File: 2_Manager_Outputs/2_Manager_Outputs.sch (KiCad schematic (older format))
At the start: 83 parts, among them J1 Jumper, J10 Jumper, J11 Jumper, J12 Jumper, J13 Jumper, J14 Jumper, J15 Jumper, J16 Jumper, J2 Jumper, J3 Jumper, J4 Jumper, J5 Jumper, J6 Jumper, J7 Jumper, J8 Jumper, J9 Jumper, P1 MCLK_EXTERNAL, P2 CONN_01X04, P3 SPI_AD5270_1, P4 CONN_01X04, P5 SPI_AD5270_2, P6 SPI_AD9833_1, P7 SPI_AD9833_2, U1 ATMEGA328P-AU, U10 ADP3334, U11 LD1117S50TR, U2 AD8421, U3 AD9833, U6 AD8421, U8 AD9833, U9 ADG819

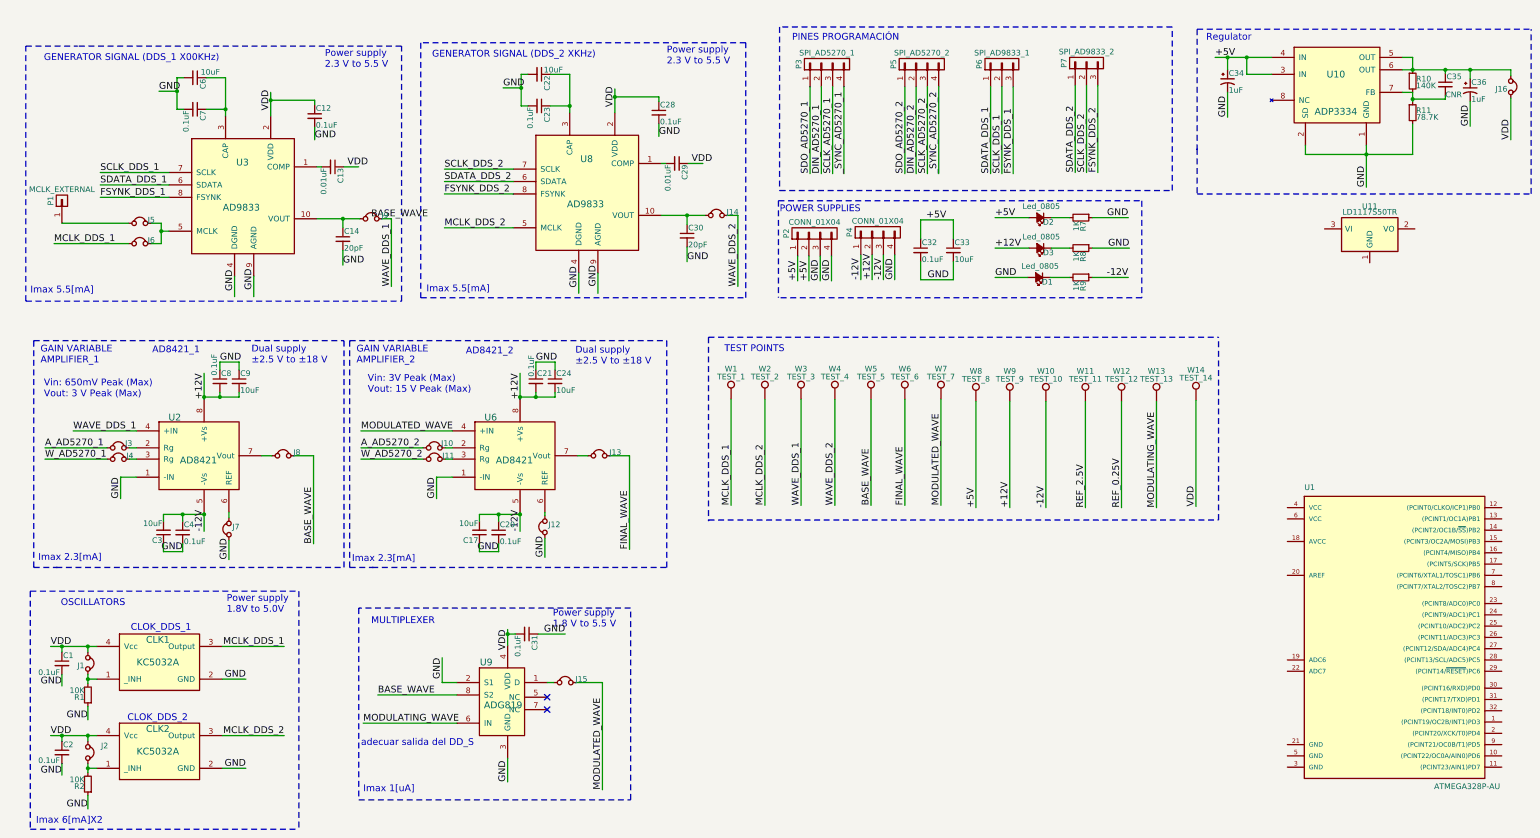
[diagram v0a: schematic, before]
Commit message: //
Plantilla para hacer tanto la pcb de manager output como la pcb de wave
generator// Separar el diseño en dos y empezar a trabajar por aparte
cada pcb
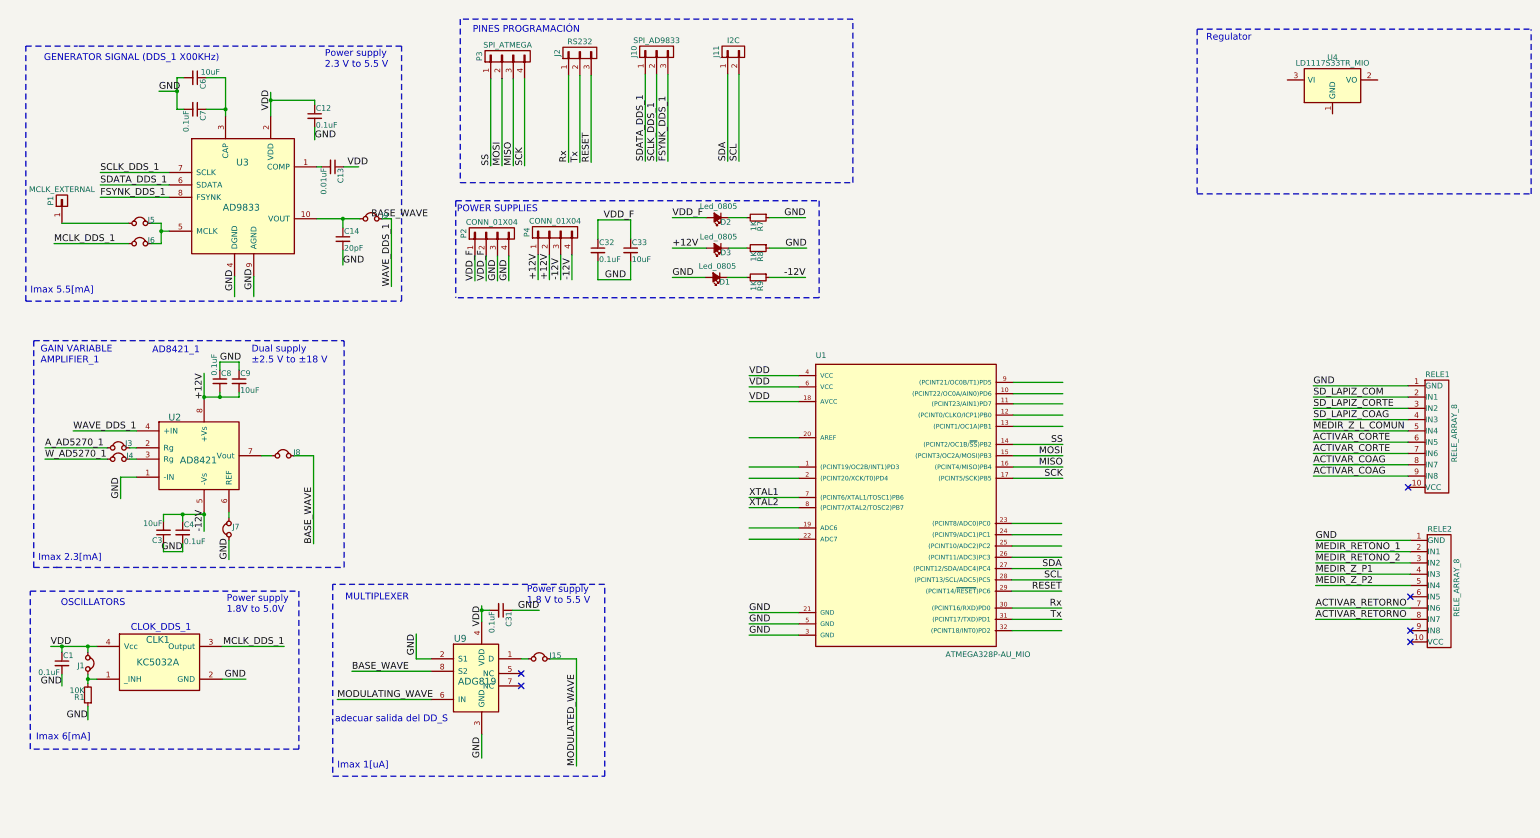
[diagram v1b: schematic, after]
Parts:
- removed C17, C24: 10uF, Capacitors_SMD:C_1206_HandSoldering, symbol 10uF
- removed C2, C20, C21, C23, C28: 0.1uF, Capacitors_SMD:C_0805_HandSoldering, symbol 0.1uF
- removed C22: 10uF, Capacitors_SMD:C_0805_HandSoldering, symbol 10uF
- removed C29: 0.01uF, Capacitors_SMD:C_0805_HandSoldering, symbol 0.01uF
- removed C30: 20pF, Capacitors_SMD:C_0805_HandSoldering, symbol 20pF
- removed C34, C36: 1uF, Capacitors_SMD:C_0805_HandSoldering, symbol CP1_Small
- removed C35: CNR, Capacitors_SMD:C_1206_HandSoldering, symbol C_Small
- removed CLK2: KC5032A, Foot_Prints_PCB_OSCILLATOR:KC5032A_Foot_Print, symbol KC5032A
- removed J10, J11, J12, J13, J14, J16, J2: Jumper, Pin_Headers:Pin_Header_Straight_1x02, symbol Jumper-RESCUE-PCB_OSCILLATOR
- removed P5: SPI_AD5270_2, Socket_Strips:Socket_Strip_Straight_1x04, symbol CONN_01X04
- removed P6: SPI_AD9833_1, Socket_Strips:Socket_Strip_Straight_1x03, symbol CONN_01X03
- removed P7: SPI_AD9833_2, Socket_Strips:Socket_Strip_Straight_1x03, symbol CONN_01X03
- removed R10: 140K, Resistors_SMD:R_0805_HandSoldering, symbol R_Small
- removed R11: 78.7K, Resistors_SMD:R_0805_HandSoldering, symbol R_Small
- removed R2: 10K, Resistors_SMD:R_0805_HandSoldering, symbol 10K
- removed U1: ATMEGA328P-AU, Housings_QFP:TQFP-32_7x7mm_Pitch0.8mm, symbol ATMEGA328P-AU
- removed U10: ADP3334, Housings_SOIC:SOIC-8_3.9x4.9mm_Pitch1.27mm, symbol ADP3334
- removed U11: LD1117S50TR, TO_SOT_Packages_SMD:SOT-223, symbol LD1117S50TR
- removed U6: AD8421, Housings_SOIC:SOIC-8_3.9x4.9mm_Pitch1.27mm, symbol AD8421
- removed U8: AD9833, Housings_SSOP:MSOP-10_3x3mm_Pitch0.5mm, symbol AD9833
- removed W1: TEST_1, Measurement_Points:Measurement_Point_Round-TH_Small, symbol TEST_1P
- removed W10: TEST_10, Measurement_Points:Measurement_Point_Round-TH_Small, symbol TEST_1P
- removed W11: TEST_11, Measurement_Points:Measurement_Point_Round-TH_Small, symbol TEST_1P
- removed W12: TEST_12, Measurement_Points:Measurement_Point_Round-TH_Small, symbol TEST_1P
- removed W13: TEST_13, Measurement_Points:Measurement_Point_Round-TH_Small, symbol TEST_1P
- removed W14: TEST_14, Measurement_Points:Measurement_Point_Round-TH_Small, symbol TEST_1P
- removed W2: TEST_2, Measurement_Points:Measurement_Point_Round-TH_Small, symbol TEST_1P
- removed W3: TEST_3, Measurement_Points:Measurement_Point_Round-TH_Small, symbol TEST_1P
- removed W4: TEST_4, Measurement_Points:Measurement_Point_Round-TH_Small, symbol TEST_1P
- removed W5: TEST_5, Measurement_Points:Measurement_Point_Round-TH_Small, symbol TEST_1P
- removed W6: TEST_6, Measurement_Points:Measurement_Point_Round-TH_Small, symbol TEST_1P
- removed W7: TEST_7, Measurement_Points:Measurement_Point_Round-TH_Small, symbol TEST_1P
- removed W8: TEST_8, Measurement_Points:Measurement_Point_Round-TH_Small, symbol TEST_1P
- removed W9: TEST_9, Measurement_Points:Measurement_Point_Round-TH_Small, symbol TEST_1P
- added J10: SPI_AD9833, Pin_Headers:Pin_Header_Straight_1x03, symbol CONN_01X03
- added J11: I2C, Pin_Headers:Pin_Header_Straight_1x02, symbol CONN_01X02
- added J2: RS232, Pin_Headers:Pin_Header_Straight_1x03, symbol CONN_01X03
- added RELE1, RELE2: RELE_ARRAY_8, Socket_Strips:Socket_Strip_Angled_1x10, symbol RELE_ARRAY_8
- added U1: ATMEGA328P-AU_MIO, Housings_QFP:TQFP-32_7x7mm_Pitch0.8mm, symbol ATMEGA328P-AU_MIO
- added U4: LD1117S33TR_MIO, TO_SOT_Packages_SMD:SOT-223, symbol LD1117S33TR_MIO
- P3: value SPI_AD5270_1 -> SPI_ATMEGA
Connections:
- net labels added: ACTIVAR_COAG, ACTIVAR_CORTE, ACTIVAR_RETORNO, MEDIR_RETONO_1, MEDIR_RETONO_2, MEDIR_Z_L_COMUN, MEDIR_Z_P1, MEDIR_Z_P2, MISO, MOSI, RESET, Rx, SCK, SCL, SDA, SD_LAPIZ_COAG, SD_LAPIZ_COM, SD_LAPIZ_CORTE, SS, Tx, VDD_F, XTAL1, XTAL2
- net labels removed: +5V, A_AD5270_2, DIN_AD5270_1, DIN_AD5270_2, FINAL_WAVE, FSYNK_DDS_2, MCLK_DDS_2, REF_0.25V, REF_2.5V, SCLK_AD5270_1, SCLK_AD5270_2, SCLK_DDS_2, SDATA_DDS_2, SDO_AD5270_1, SDO_AD5270_2, WAVE_DDS_2, W_AD5270_2, _SYNC_AD5270_1, _SYNC_AD5270_2
- wire segments 206 -> 158
- no-connect marks 2 -> 6
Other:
- note added: "Imax 6[mA]"
- note removed: "AD8421_2"
- note removed: "CLOK_DDS_2"
- note removed: "GAIN VARIABLE\nAMPLIFIER_2"
- note removed: "GENERATOR SIGNAL (DDS_2 XKHz)\n"
- note removed: "Imax 6[mA]X2"
- note removed: "TEST POINTS"
- note removed: "Vin: 3V Peak (Max)\nVout: 15 V Peak (Max)"
- note removed: "Vin: 650mV Peak (Max)\nVout: 3 V Peak (Max)"
- moved on the sheet: C31, C32, C33, D1, D2, D3, J15, P2, P3, P4, R7, R8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

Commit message: //
Dejo el esquematico solo con las cosas del manager Outut
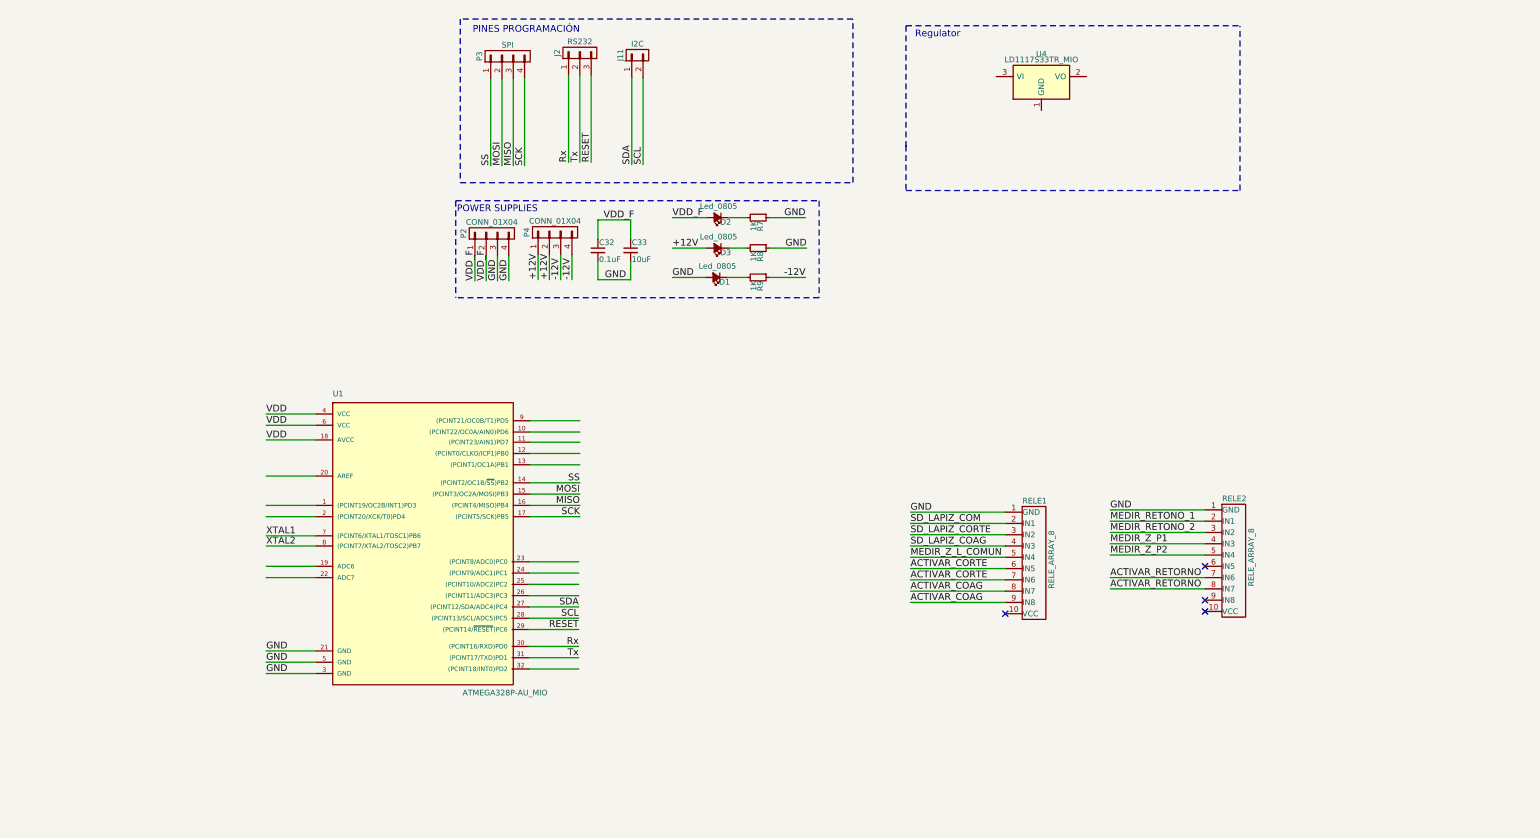
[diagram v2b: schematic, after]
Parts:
- removed C1, C12, C31, C4, C7, C8: 0.1uF, Capacitors_SMD:C_0805_HandSoldering, symbol 0.1uF
- removed C13: 0.01uF, Capacitors_SMD:C_0805_HandSoldering, symbol 0.01uF
- removed C14: 20pF, Capacitors_SMD:C_0805_HandSoldering, symbol 20pF
- removed C3, C9: 10uF, Capacitors_SMD:C_1206_HandSoldering, symbol 10uF
- removed C6: 10uF, Capacitors_SMD:C_0805_HandSoldering, symbol 10uF
- removed CLK1: KC5032A, Foot_Prints_PCB_OSCILLATOR:KC5032A_Foot_Print, symbol KC5032A
- removed J1, J15, J3, J4, J5, J6, J7, J8, J9: Jumper, Pin_Headers:Pin_Header_Straight_1x02, symbol Jumper-RESCUE-PCB_OSCILLATOR
- removed J10: SPI_AD9833, Pin_Headers:Pin_Header_Straight_1x03, symbol CONN_01X03
- removed P1: MCLK_EXTERNAL, Socket_Strips:Socket_Strip_Straight_1x01, symbol CONN_01X01
- removed R1: 10K, Resistors_SMD:R_0805_HandSoldering, symbol 10K
- removed U2: AD8421, Housings_SOIC:SOIC-8_3.9x4.9mm_Pitch1.27mm, symbol AD8421
- removed U3: AD9833, Housings_SSOP:MSOP-10_3x3mm_Pitch0.5mm, symbol AD9833
- removed U9: ADG819, Housings_SSOP:MSOP-8_3x3mm_Pitch0.65mm, symbol ADG819
- P3: value SPI_ATMEGA -> SPI
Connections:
- net labels removed: A_AD5270_1, BASE_WAVE, FSYNK_DDS_1, MCLK_DDS_1, MODULATED_WAVE, MODULATING_WAVE, SCLK_DDS_1, SDATA_DDS_1, WAVE_DDS_1, W_AD5270_1
- wire segments 158 -> 80
- no-connect marks 6 -> 4
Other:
- note removed: "AD8421_1"
- note removed: "CLOK_DDS_1"
- note removed: "Dual supply\n±2.5 V to ±18 V"
- note removed: "GAIN VARIABLE\nAMPLIFIER_1"
- note removed: "GENERATOR SIGNAL (DDS_1 X00KHz)\n"
- note removed: "Imax 1[uA]"
- note removed: "Imax 2.3[mA]"
- note removed: "Imax 5.5[mA]"
- note removed: "Imax 6[mA]"
- note removed: "MULTIPLEXER"
- note removed: "OSCILLATORS"
- note removed: "Power supply\n1.8 V to 5.5 V"
- note removed: "Power supply\n1.8V to 5.0V"
- note removed: "Power supply\n2.3 V to 5.5 V"
- note removed: "adecuar salida del DD_S"
- moved on the sheet: J11, RELE1, RELE2, U1, U4

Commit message: //
//
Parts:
- removed P2, P4: CONN_01X04, Socket_Strips:Socket_Strip_Straight_1x04, symbol CONN_01X04
- removed R8, R9: 1K, Resistors_SMD:R_0805_HandSoldering, symbol 1K
- added C1, C10, C3, C4, C5: 0.1uF, Resistors_SMD:R_0805_HandSoldering, symbol 0.1uF
- added C2: 10uF, Resistors_SMD:R_0805_HandSoldering, symbol 10uF
- added C6, C7: 8pF, Resistors_SMD:R_0805_HandSoldering, symbol 20pF
- added C8: 0.1uF, Capacitors_SMD:C_0805_HandSoldering, symbol 0.1uF
- added C9: 10uF, Capacitors_SMD:C_0805_HandSoldering, symbol 10uF
- added J1: VDD 12V, Foot_Prints_Manager_Outputs:SUPPLY_12V, symbol CONN_01X02
- added J3: VDD 5V, Foot_Prints_Manager_Outputs:SUPPLY_5V, symbol CONN_01X02
- added J4: SPEAKER, Socket_Strips:Socket_Strip_Straight_1x02, symbol CONN_01X02
- added J5: RESET, Foot_Prints_Manager_Outputs:RESET_CONNECTOR, symbol CONN_01X02
- added JP1: J_Aref, Resistors_SMD:R_0805_HandSoldering, symbol Jumper_NC_Small
- added JP2: J_+12V, Socket_Strips:Socket_Strip_Straight_1x02, symbol Jumper_NC_Small
- added JP3: J_VDD, Socket_Strips:Socket_Strip_Straight_1x02, symbol Jumper_NC_Small
- added R1, R2: 1K, Resistors_SMD:R_0805_HandSoldering, symbol 1K
- added R3: 10K, Resistors_SMD:R_0805_HandSoldering, symbol 10K
- added RELE3: RELE_ARRAY_8, Foot_Prints_Manager_Outputs:Socket_Strip_Straight_2x10_Mio_2, symbol RELE_ARRAY_8
- added SW1: Reset, Huellas:KPT_1187B, symbol SW_Push
- added Y1: Crystal, Huellas:Crystal_SMD_XRCHA_Murata_Serie_W2,5mm_L2,0mm, symbol Crystal_Small
- D1: value Led_0805 -> 5V
- D2: value Led_0805 -> 12V
- D3: value Led_0805 -> VDD
- J11: footprint Pin_Headers:Pin_Header_Straight_1x02 -> Foot_Prints_Manager_Outputs:I2C_2X4
- J2: footprint Pin_Headers:Pin_Header_Straight_1x03 -> Foot_Prints_Manager_Outputs:RS232
- P3: footprint Socket_Strips:Socket_Strip_Straight_1x04 -> Foot_Prints_Manager_Outputs:SPI_CONNECTOR
- RELE1: footprint Socket_Strips:Socket_Strip_Angled_1x10 -> Foot_Prints_Manager_Outputs:Socket_Strip_Straight_2x10_Mio_2
- RELE2: footprint Socket_Strips:Socket_Strip_Angled_1x10 -> Foot_Prints_Manager_Outputs:Socket_Strip_Straight_2x10_Mio
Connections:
- net labels added: +5V, DTR, SPEAKER
- net labels removed: -12V, VDD_F
- wire segments 80 -> 125
- no-connect marks 4 -> 9
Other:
- note added: "CRYSTAL \nOSCILLATOR"
- note added: "DECUPLING CAPACITORS"
- note added: "DIGITAL BUSES AND CONNECTORS"
- note added: "INDICATORS LEDS"
- note added: "Microcontroller"
- note added: "RELES"
- note added: "RESET"
- note removed: "PINES PROGRAMACIÓN"
- moved on the sheet: C32, C33, D2, J11, J2, P3, R7, RELE1, RELE2, U1, U4

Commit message: //
//
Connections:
- net SCL: now also J11.1 (P1); no longer J11.2 (P2)
- net SDA: now also J11.2 (P2); no longer J11.1 (P1)
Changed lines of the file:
@@
 	0    -1   -1   0
 $EndComp
+Text Label 1890 1880 1    60   ~ 0
+SDA
 Text Label 1790 1880 1    60   ~ 0
-SDA
-Text Label 1890 1880 1    60   ~ 0
 SCL
 Text Label 4620 3990 2    60   ~ 0

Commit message: //
//
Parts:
- added D4: TEST, Resistors_SMD:R_0805_HandSoldering, symbol Led_0805
- added JP4: J_TEST, Resistors_SMD:R_0805_HandSoldering, symbol Jumper_NC_Small
- added R4: 1K, Resistors_SMD:R_0805_HandSoldering, symbol 1K
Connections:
- net GND: now also R4.1
- net SPEAKER: now also JP4.1
- new net: D4.2 (A), JP4.2
- new net: D4.1 (K), R4.2
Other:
- note added: "TEST LED"
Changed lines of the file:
@@
 Text Label 6460 690  3    60   ~ 0
 DTR
+$Comp
+L Jumper_NC_Small JP4
+U 1 1 59D5CEEF
+P 1440 2420
+F 0 "JP4" H 1440 2500 50  0000 C CNN
+F 1 "J_TEST" H 1450 2360 50  0000 C CNN
+F 2 "Resistors_SMD:R_0805_HandSoldering" H 1440 2420 50  0001 C CNN
+F 3 "" H 1440 2420 50  0001 C CNN
+	1    1440 2420
+	1    0    0    -1
+$EndComp
+Text Label 2820 2420 2    60   ~ 0
+GND
+$Comp
+L 1K R4
+U 1 1 59D5D6B8
+P 2400 2420
+F 0 "R4" H 2430 2440 50  0000 L CNN
+F 1 "1K" H 2430 2380 50  0000 L CNN
+F 2 "Resistors_SMD:R_0805_HandSoldering" H 2330 2340 50  0001 C CNN
+F 3 "" H 2430 2440 50  0000 C CNN
+F 4 "P21019TR-ND" H 2530 2540 60  0001 C CNN "RES SMD 1K OHM 0.5% 1/4W 0805"
+	1    2400 2420
+	0    1    1    0
+$EndComp
+$Comp
+L Led_0805 D4
+U 1 1 59D5D6BF
+P 2040 2420
+F 0 "D4" H 1920 2460 50  0000 L CNN
+F 1 "TEST" H 1950 2340 50  0000 L CNN
+F 2 "Resistors_SMD:R_0805_HandSoldering" H 1890 2445 50  0001 C CNN
+F 3 "" H 1990 2545 50  0000 C CNN
+F 4 "475-1410-2-ND" H 2090 2645 60  0001 C CNN "Digi-Key Part Number"
+	1    2040 2420
+	-1   0    0    1
+$EndComp
+Wire Wire Line
+	1540 2420 1940 2420
+Wire Wire Line
+	2140 2420 2300 2420
+Wire Wire Line
+	2500 2420 2820 2420
+Wire Wire Line
+	900  2420 1340 2420
+Text Label 900  2420 0    60   ~ 0
+SPEAKER
+Wire Notes Line
+	660  2080 660  2650
+Wire Notes Line
+	660  2650 3090 2650
+Wire Notes Line
+	3090 2650 3090 2080
+Wire Notes Line
+	3090 2080 660  2080
+Text Notes 750  2190 0    60   ~ 0
+TEST LED
 $EndSCHEMATC

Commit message: //
//
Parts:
- C6, C7: footprint Resistors_SMD:R_0805_HandSoldering -> Capacitors_SMD:C_0402
- JP4: footprint Resistors_SMD:R_0805_HandSoldering -> Pin_Headers:Pin_Header_Straight_1x02
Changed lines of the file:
@@
 F 0 "C6" H 6170 2090 50  0000 L CNN
 F 1 "8pF" H 6170 1940 50  0000 L CNN
-F 2 "Resistors_SMD:R_0805_HandSoldering" H 6070 1990 50  0001 C CNN
+F 2 "Capacitors_SMD:C_0402" H 6070 1990 50  0001 C CNN
 F 3 "" H 6170 2090 50  0001 C CNN
 F 4 "478-3735-2-ND" H 6270 2190 60  0001 C CNN "100V"
@@
 F 0 "C7" H 6970 2090 50  0000 L CNN
 F 1 "8pF" H 6970 1940 50  0000 L CNN
-F 2 "Resistors_SMD:R_0805_HandSoldering" H 6870 1990 50  0001 C CNN
+F 2 "Capacitors_SMD:C_0402" H 6870 1990 50  0001 C CNN
 F 3 "" H 6970 2090 50  0001 C CNN
 F 4 "478-3735-2-ND" H 7070 2190 60  0001 C CNN "100V"
@@
 F 0 "JP4" H 1440 2500 50  0000 C CNN
 F 1 "J_TEST" H 1450 2360 50  0000 C CNN
-F 2 "Resistors_SMD:R_0805_HandSoldering" H 1440 2420 50  0001 C CNN
+F 2 "Pin_Headers:Pin_Header_Straight_1x02" H 1440 2420 50  0001 C CNN
 F 3 "" H 1440 2420 50  0001 C CNN
 	1    1440 2420

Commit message: Revert "//"
This reverts commit a491b2ffacc572f737e67cceefcc72cf1d6daf07.
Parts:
- C6, C7: footprint Capacitors_SMD:C_0402 -> Resistors_SMD:R_0805_HandSoldering
- JP4: footprint Pin_Headers:Pin_Header_Straight_1x02 -> Resistors_SMD:R_0805_HandSoldering
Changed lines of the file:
@@
 F 0 "C6" H 6170 2090 50  0000 L CNN
 F 1 "8pF" H 6170 1940 50  0000 L CNN
-F 2 "Capacitors_SMD:C_0402" H 6070 1990 50  0001 C CNN
+F 2 "Resistors_SMD:R_0805_HandSoldering" H 6070 1990 50  0001 C CNN
 F 3 "" H 6170 2090 50  0001 C CNN
 F 4 "478-3735-2-ND" H 6270 2190 60  0001 C CNN "100V"
@@
 F 0 "C7" H 6970 2090 50  0000 L CNN
 F 1 "8pF" H 6970 1940 50  0000 L CNN
-F 2 "Capacitors_SMD:C_0402" H 6870 1990 50  0001 C CNN
+F 2 "Resistors_SMD:R_0805_HandSoldering" H 6870 1990 50  0001 C CNN
 F 3 "" H 6970 2090 50  0001 C CNN
 F 4 "478-3735-2-ND" H 7070 2190 60  0001 C CNN "100V"
@@
 F 0 "JP4" H 1440 2500 50  0000 C CNN
 F 1 "J_TEST" H 1450 2360 50  0000 C CNN
-F 2 "Pin_Headers:Pin_Header_Straight_1x02" H 1440 2420 50  0001 C CNN
+F 2 "Resistors_SMD:R_0805_HandSoldering" H 1440 2420 50  0001 C CNN
 F 3 "" H 1440 2420 50  0001 C CNN
 	1    1440 2420
